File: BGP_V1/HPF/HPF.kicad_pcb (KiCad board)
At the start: 2 copper layers, 30 x 30 mm, 12 parts, among them P1 CONN_01X05, P2 CONN_01X06, U1 OPA2170

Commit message: Fixups
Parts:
- P2: moved to B.Cu
- moved P2 5.00 mm to (152.5, 53.0)
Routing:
- net /VF_1: track 11.3 -> 18.6 mm
- net /VP_1: track 29.4 -> 26.7 mm
- net Earth: track 2.40 -> 4.90 mm

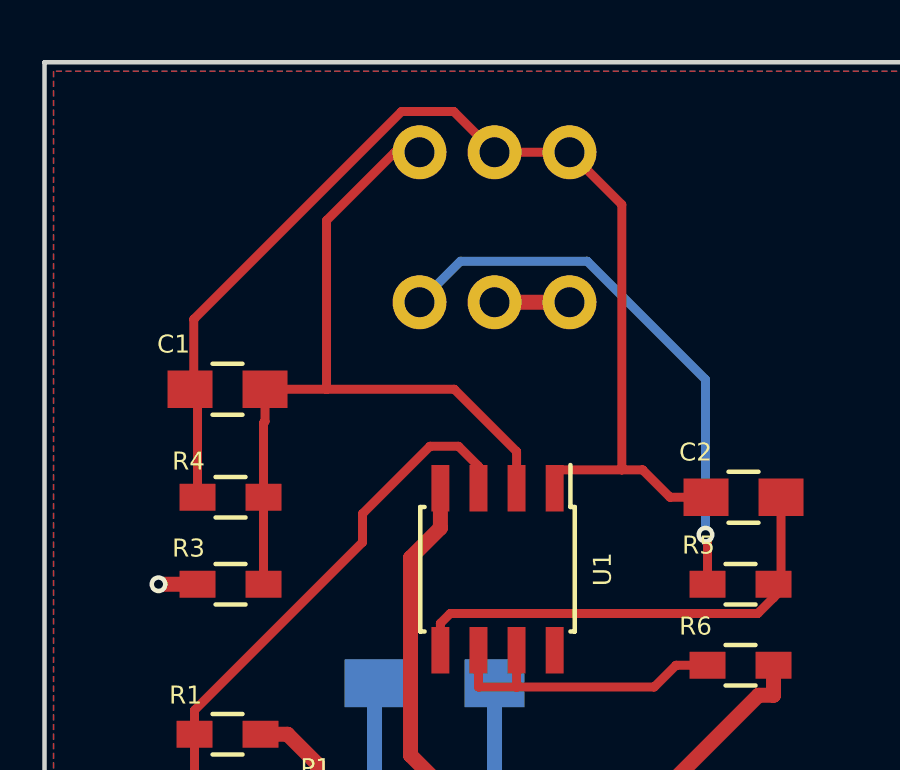
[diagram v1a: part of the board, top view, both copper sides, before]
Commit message: Pot fixups for silkscreen overlap
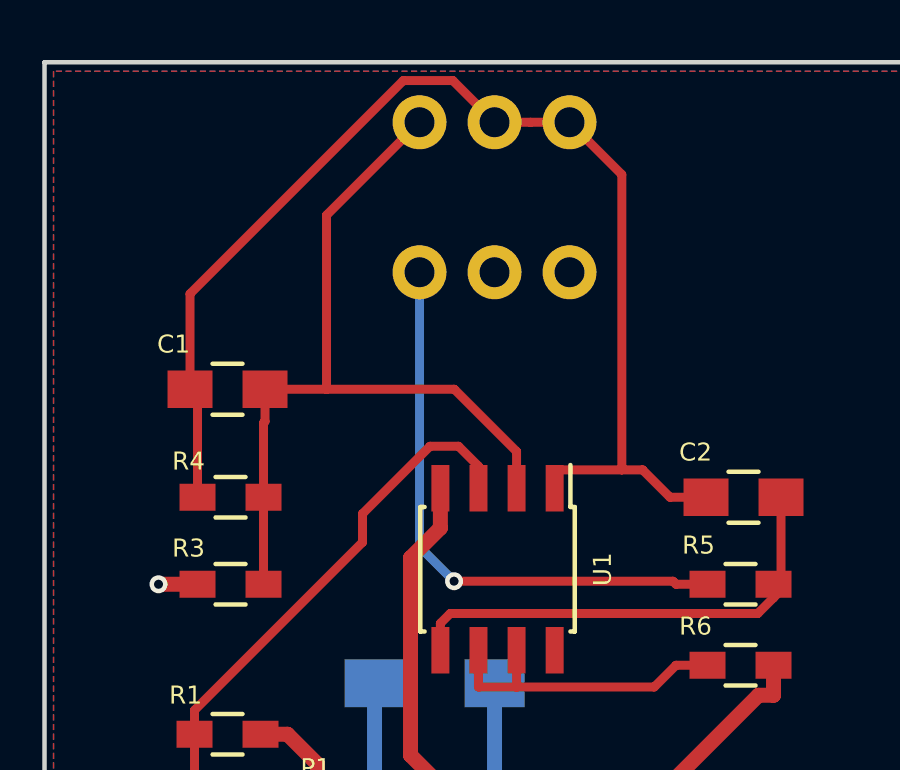
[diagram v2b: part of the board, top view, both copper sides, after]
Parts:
- R4: value 20k -> 24.9k
- moved P2 1.00 mm to (152.5, 52.0)
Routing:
- net Earth: track 4.90 -> 2.40 mm
- net /VP_2: track 39.5 -> 41.4 mm
- net /VF_1: track 18.6 -> 19.3 mm
- net /VP_1: track 26.7 -> 27.2 mm

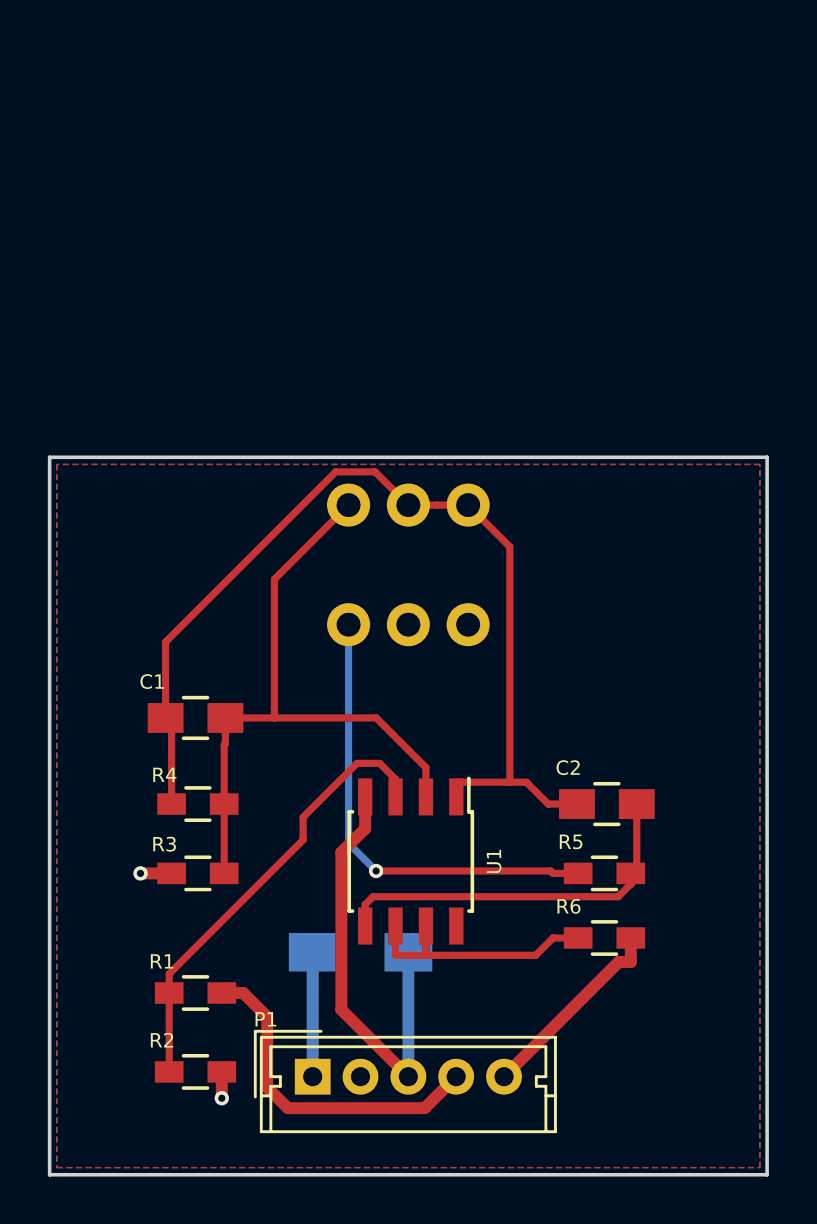
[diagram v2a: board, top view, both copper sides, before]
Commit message: Concentric pot fixups for 0_BT Stack and 1_HPF
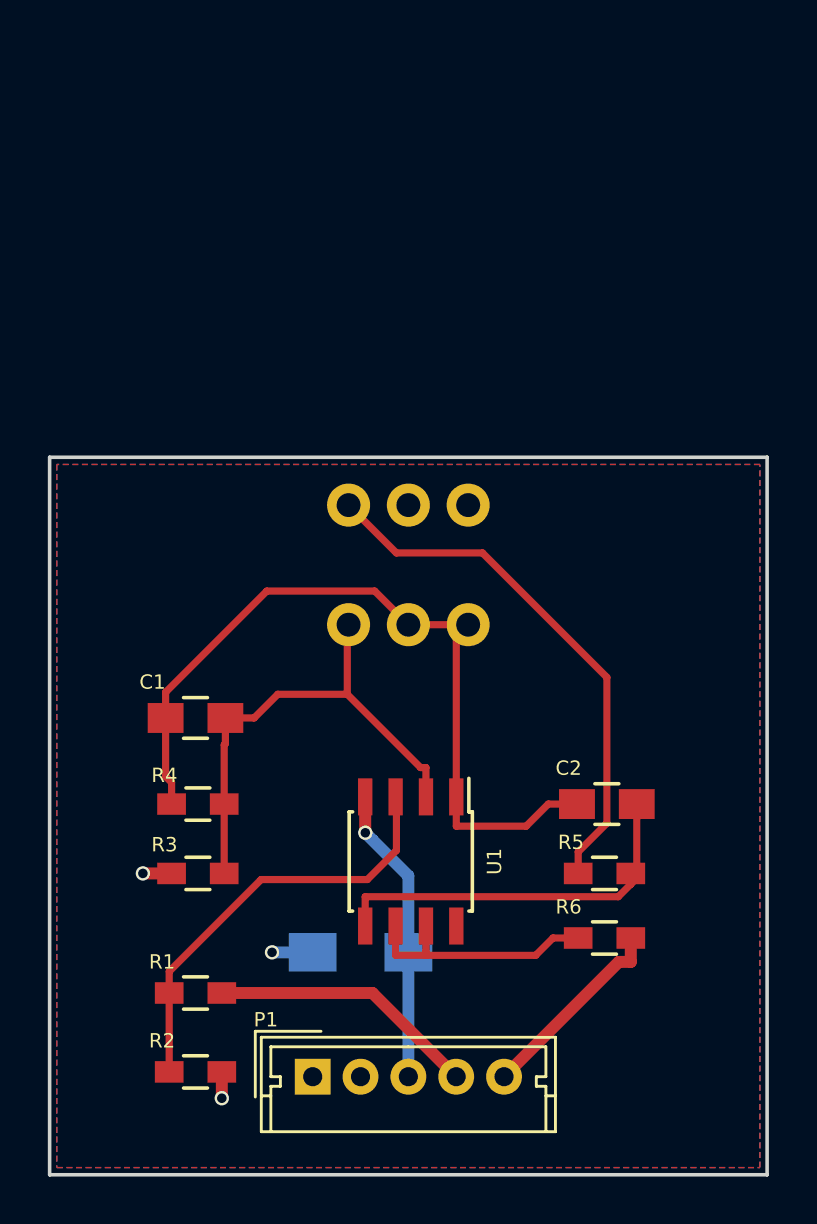
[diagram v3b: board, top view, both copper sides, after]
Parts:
- removed P2: CONN_01X06, LIBS:Potentiometer_Alps_RK097_Double_Vertical_Dual_Shaft
- added RV1: DUAL_POT, LIBS:Potentiometer_Alps_RK097_Double_Vertical_Dual_Shaft, B.Cu at (152.5, 52.0)
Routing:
- net /VP_2: track 41.4 -> 33.6 mm
- net /VP_1: track 27.2 -> 20.7 mm
- net /V-: track 18.5 -> 12.4 mm, vias 0 -> 1
- net /V+: track 5.20 -> 1.70 mm, vias 0 -> 1
- net /VF_1: track 19.3 -> 22.5 mm, vias 1 -> 0
- net /IN: track 14.1 -> 11.2 mm
- net Net-(R1-Pad1): track 18.8 -> 18.1 mm

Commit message: BOM for V1 BGP
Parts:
- moved C3 0.14 mm to (153.1, 70.6)
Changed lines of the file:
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@@
   (page A4)
   (layers
-    (0 F.Cu signal)
+    (0 F.Cu signal hide)
     (31 B.Cu signal)
     (32 B.Adhes user)
@@
     )
   )
-  (module Capacitors_SMD:C_1206_HandSoldering (layer B.Cu)
-    (at 153 70.7)
-    (descr "Capacitor SMD 1206, hand soldering")
-    (tags "capacitor 1206")
-    (attr smd)
-    (fp_text reference C3 (at 2.6 -1.6) (layer B.SilkS)
-      (effects (font (size 0.6 0.6) (thickness 0.15)) (justify mirror))
-    )
-    (fp_text value 10u (at 0 -2.3) (layer B.Fab) hide
-      (effects (font (size 0.6 0.6) (thickness 0.15)) (justify mirror))
-    )
-    (fp_line (start -3.3 1.15) (end 3.3 1.15) (layer B.CrtYd) (width 0.05))
-    (fp_line (start -3.3 -1.15) (end 3.3 -1.15) (layer B.CrtYd) (width 0.05))
-    (fp_line (start -3.3 1.15) (end -3.3 -1.15) (layer B.CrtYd) (width 0.05))
-    (fp_line (start 3.3 1.15) (end 3.3 -1.15) (layer B.CrtYd) (width 0.05))
-    (fp_line (start 1 1.025) (end -1 1.025) (layer B.SilkS) (width 0.15))
-    (fp_line (start -1 -1.025) (end 1 -1.025) (layer B.SilkS) (width 0.15))
-    (pad 1 smd rect (at -2 0) (size 2 1.6) (layers B.Cu B.Paste B.Mask)
-      (net 4 /V+))
-    (pad 2 smd rect (at 2 0) (size 2 1.6) (layers B.Cu B.Paste B.Mask)
-      (net 5 /V-))
-    (model Capacitors_SMD.3dshapes/C_1206_HandSoldering.wrl
-      (at (xyz 0 0 0))
-      (scale (xyz 1 1 1))
-      (rotate (xyz 0 0 0))
-    )
-  )
   (module Resistors_SMD:R_0603_HandSoldering (layer F.Cu)
     (at 146.1 72.4)
@@
       (rotate (xyz 0 0 0))
     )
+  )
+  (module Capacitors_SMD:C_1206_HandSoldering (layer B.Cu)
+    (at 153.1 70.6)
+    (descr "Capacitor SMD 1206, hand soldering")
+    (tags "capacitor 1206")
+    (attr smd)
+    (fp_text reference C3 (at 2.8 -1.6) (layer B.SilkS)
+      (effects (font (size 0.6 0.6) (thickness 0.15)) (justify mirror))
+    )
+    (fp_text value 10u (at 0 -2.3) (layer B.Fab) hide
+      (effects (font (size 0.6 0.6) (thickness 0.15)) (justify mirror))
+    )
+    (fp_line (start -3.3 1.15) (end 3.3 1.15) (layer B.CrtYd) (width 0.05))
+    (fp_line (start -3.3 -1.15) (end 3.3 -1.15) (layer B.CrtYd) (width 0.05))
+    (fp_line (start -3.3 1.15) (end -3.3 -1.15) (layer B.CrtYd) (width 0.05))
+    (fp_line (start 3.3 1.15) (end 3.3 -1.15) (layer B.CrtYd) (width 0.05))
+    (fp_line (start 1 1.025) (end -1 1.025) (layer B.SilkS) (width 0.15))
+    (fp_line (start -1 -1.025) (end 1 -1.025) (layer B.SilkS) (width 0.15))
+    (pad 1 smd rect (at -2 0) (size 2 1.6) (layers B.Cu B.Paste B.Mask)
+      (net 4 /V+))
+    (pad 2 smd rect (at 2 0) (size 2 1.6) (layers B.Cu B.Paste B.Mask)
+      (net 5 /V-))
+    (model Capacitors_SMD.3dshapes/C_1206_HandSoldering.wrl
+      (at (xyz 0 0 0))
+      (scale (xyz 1 1 1))
+      (rotate (xyz 0 0 0))
+    )

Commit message: Slight changes to Port layer placement - gerbers done
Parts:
- P1: moved to B.Cu
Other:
- board text added: "+"
- board text added: "-"
- board text added: "G"
- board text added: "I"
- board text added: "O"
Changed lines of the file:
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@@
     (links 26)
     (no_connects 0)
-    (area 139.924999 49.424999 170.075001 81.955)
+    (area 139.924999 49.424999 170.075001 80.075001)
     (thickness 1.6)
-    (drawings 9)
+    (drawings 14)
     (tracks 71)
     (zones 0)
@@
   (page A4)
   (layers
-    (0 F.Cu signal hide)
+    (0 F.Cu signal)
     (31 B.Cu signal)
     (32 B.Adhes user)
@@
     )
   )
-  (module Connectors_Molex:Molex_MicroLatch-53253-0570_05x2.00mm_Straight (layer F.Cu)
+  (module Connectors_Molex:Molex_MicroLatch-53253-0570_05x2.00mm_Straight (layer B.Cu)
     (at 151 75.9)
     (descr "Molex Micro-Latch connector, PN:53253-0570, top entry type, through hole")
     (tags "conn molex micro latch")
-    (fp_text reference P1 (at -1.96 -2.38) (layer F.SilkS)
-      (effects (font (size 0.6 0.6) (thickness 0.15)))
-    )
-    (fp_text value CONN_01X05 (at 3.63 5.2) (layer F.Fab) hide
-      (effects (font (size 0.6 0.6) (thickness 0.15)))
-    )
-    (fp_line (start -2 -1.5) (end -2 2.15) (layer F.Fab) (width 0.1))
-    (fp_line (start -2 2.15) (end 10 2.15) (layer F.Fab) (width 0.1))
-    (fp_line (start 10 2.15) (end 10 -1.5) (layer F.Fab) (width 0.1))
-    (fp_line (start 10 -1.5) (end -2 -1.5) (layer F.Fab) (width 0.1))
-    (fp_line (start -2.6 -2.1) (end -2.6 2.75) (layer F.CrtYd) (width 0.05))
-    (fp_line (start -2.6 2.75) (end 10.65 2.75) (layer F.CrtYd) (width 0.05))
-    (fp_line (start 10.65 2.75) (end 10.65 -2.1) (layer F.CrtYd) (width 0.05))
-    (fp_line (start 10.65 -2.1) (end -2.6 -2.1) (layer F.CrtYd) (width 0.05))
-    (fp_line (start -2.15 -1.65) (end -2.15 2.3) (layer F.SilkS) (width 0.12))
-    (fp_line (start -2.15 2.3) (end 10.15 2.3) (layer F.SilkS) (width 0.12))
-    (fp_line (start 10.15 2.3) (end 10.15 -1.65) (layer F.SilkS) (width 0.12))
-    (fp_line (start 10.15 -1.65) (end -2.15 -1.65) (layer F.SilkS) (width 0.12))
-    (fp_line (start 0.35 -1.9) (end -2.4 -1.9) (layer F.SilkS) (width 0.12))
-    (fp_line (start -2.4 -1.9) (end -2.4 0.85) (layer F.SilkS) (width 0.12))
-    (fp_line (start 0.35 -1.9) (end -2.4 -1.9) (layer F.Fab) (width 0.1))
-    (fp_line (start -2.4 -1.9) (end -2.4 0.85) (layer F.Fab) (width 0.1))
-    (fp_line (start -2.15 0.8) (end -1.75 0.8) (layer F.SilkS) (width 0.12))
-    (fp_line (start 10.15 0.8) (end 9.75 0.8) (layer F.SilkS) (width 0.12))
-    (fp_line (start 4 -1.25) (end -1.75 -1.25) (layer F.SilkS) (width 0.12))
-    (fp_line (start -1.75 -1.25) (end -1.75 0) (layer F.SilkS) (width 0.12))
-    (fp_line (start -1.75 0) (end -1.35 0) (layer F.SilkS) (width 0.12))
-    (fp_line (start -1.35 0) (end -1.35 0.4) (layer F.SilkS) (width 0.12))
-    (fp_line (start -1.35 0.4) (end -1.75 0.4) (layer F.SilkS) (width 0.12))
-    (fp_line (start -1.75 0.4) (end -1.75 2.3) (layer F.SilkS) (width 0.12))
-    (fp_line (start 4 -1.25) (end 9.75 -1.25) (layer F.SilkS) (width 0.12))
-    (fp_line (start 9.75 -1.25) (end 9.75 0) (layer F.SilkS) (width 0.12))
-    (fp_line (start 9.75 0) (end 9.35 0) (layer F.SilkS) (width 0.12))
-    (fp_line (start 9.35 0) (end 9.35 0.4) (layer F.SilkS) (width 0.12))
-    (fp_line (start 9.35 0.4) (end 9.75 0.4) (layer F.SilkS) (width 0.12))
-    (fp_line (start 9.75 0.4) (end 9.75 2.3) (layer F.SilkS) (width 0.12))
-    (fp_text user %R (at 4 1.5) (layer F.Fab) hide
-      (effects (font (size 0.6 0.6) (thickness 0.15)))
+    (fp_text reference P1 (at -2.5 2.38) (layer B.SilkS)
+      (effects (font (size 0.6 0.6) (thickness 0.15)) (justify mirror))
+    )
+    (fp_text value CONN_01X05 (at 3.63 -5.2) (layer B.Fab) hide
+      (effects (font (size 0.6 0.6) (thickness 0.15)) (justify mirror))
+    )
+    (fp_line (start -2 1.5) (end -2 -2.15) (layer B.Fab) (width 0.1))
+    (fp_line (start -2 -2.15) (end 10 -2.15) (layer B.Fab) (width 0.1))
+    (fp_line (start 10 -2.15) (end 10 1.5) (layer B.Fab) (width 0.1))
+    (fp_line (start 10 1.5) (end -2 1.5) (layer B.Fab) (width 0.1))
+    (fp_line (start -2.6 2.1) (end -2.6 -2.75) (layer B.CrtYd) (width 0.05))
+    (fp_line (start -2.6 -2.75) (end 10.65 -2.75) (layer B.CrtYd) (width 0.05))
+    (fp_line (start 10.65 -2.75) (end 10.65 2.1) (layer B.CrtYd) (width 0.05))
+    (fp_line (start 10.65 2.1) (end -2.6 2.1) (layer B.CrtYd) (width 0.05))
+    (fp_line (start -2.15 1.65) (end -2.15 -2.3) (layer B.SilkS) (width 0.12))
+    (fp_line (start -2.15 -2.3) (end 10.15 -2.3) (layer B.SilkS) (width 0.12))
+    (fp_line (start 10.15 -2.3) (end 10.15 1.65) (layer B.SilkS) (width 0.12))
+    (fp_line (start 10.15 1.65) (end -2.15 1.65) (layer B.SilkS) (width 0.12))
+    (fp_line (start 0.35 1.9) (end -2.4 1.9) (layer B.SilkS) (width 0.12))
+    (fp_line (start -2.4 1.9) (end -2.4 -0.85) (layer B.SilkS) (width 0.12))
+    (fp_line (start 0.35 1.9) (end -2.4 1.9) (layer B.Fab) (width 0.1))
+    (fp_line (start -2.4 1.9) (end -2.4 -0.85) (layer B.Fab) (width 0.1))
+    (fp_line (start -2.15 -0.8) (end -1.75 -0.8) (layer B.SilkS) (width 0.12))
+    (fp_line (start 10.15 -0.8) (end 9.75 -0.8) (layer B.SilkS) (width 0.12))
+    (fp_line (start 4 1.25) (end -1.75 1.25) (layer B.SilkS) (width 0.12))
+    (fp_line (start -1.75 1.25) (end -1.75 0) (layer B.SilkS) (width 0.12))
+    (fp_line (start -1.75 0) (end -1.35 0) (layer B.SilkS) (width 0.12))
+    (fp_line (start -1.35 0) (end -1.35 -0.4) (layer B.SilkS) (width 0.12))
+    (fp_line (start -1.35 -0.4) (end -1.75 -0.4) (layer B.SilkS) (width 0.12))
+    (fp_line (start -1.75 -0.4) (end -1.75 -2.3) (layer B.SilkS) (width 0.12))
+    (fp_line (start 4 1.25) (end 9.75 1.25) (layer B.SilkS) (width 0.12))
+    (fp_line (start 9.75 1.25) (end 9.75 0) (layer B.SilkS) (width 0.12))
+    (fp_line (start 9.75 0) (end 9.35 0) (layer B.SilkS) (width 0.12))
+    (fp_line (start 9.35 0) (end 9.35 -0.4) (layer B.SilkS) (width 0.12))
+    (fp_line (start 9.35 -0.4) (end 9.75 -0.4) (layer B.SilkS) (width 0.12))
+    (fp_line (start 9.75 -0.4) (end 9.75 -2.3) (layer B.SilkS) (width 0.12))
+    (fp_text user %R (at 4 -1.5) (layer B.Fab) hide
+      (effects (font (size 0.6 0.6) (thickness 0.15)) (justify mirror))
     )
     (pad 1 thru_hole rect (at 0 0) (size 1.5 1.5) (drill 0.8) (layers *.Cu *.Mask)
@@
     )
   )
+  (gr_text O (at 159 78.8) (layer B.SilkS)
+    (effects (font (size 0.6 0.6) (thickness 0.15)) (justify mirror))
+  )
+  (gr_text I (at 157 78.8) (layer B.SilkS)
+    (effects (font (size 0.6 0.6) (thickness 0.15)) (justify mirror))
+  )
+  (gr_text - (at 155 78.7) (layer B.SilkS)
+    (effects (font (size 0.6 0.6) (thickness 0.15)) (justify mirror))
+  )
+  (gr_text G (at 153 78.8) (layer B.SilkS)
+    (effects (font (size 0.6 0.6) (thickness 0.15)) (justify mirror))
+  )
+  (gr_text + (at 151 78.8) (layer B.SilkS)
+    (effects (font (size 0.6 0.6) (thickness 0.15)) (justify mirror))
+  )
   (gr_text "BGP V1.0\nHigh Pass Filter" (at 144.2 51.4) (layer B.SilkS)

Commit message: Slight changes to Port layer placement - gerbers done
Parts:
- moved P1 1.40 mm to (151.0, 77.3)
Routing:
- net /OUT: track 8.29 -> 10.0 mm
- net /V-: track 12.4 -> 14.0 mm
- net /IN: track 11.2 -> 11.8 mm
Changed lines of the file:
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@@
     (thickness 1.6)
     (drawings 14)
-    (tracks 71)
+    (tracks 73)
     (zones 0)
     (modules 12)
@@
   )
   (module Connectors_Molex:Molex_MicroLatch-53253-0570_05x2.00mm_Straight (layer B.Cu)
-    (at 151 75.9)
+    (at 151 77.3)
     (descr "Molex Micro-Latch connector, PN:53253-0570, top entry type, through hole")
     (tags "conn molex micro latch")
-    (fp_text reference P1 (at -2.5 2.38) (layer B.SilkS)
+    (fp_text reference P1 (at 11.2 -1.9) (layer B.SilkS)
       (effects (font (size 0.6 0.6) (thickness 0.15)) (justify mirror))
     )
@@
     )
   )
-  (gr_text O (at 159 78.8) (layer B.SilkS)
+  (gr_text O (at 159 74) (layer B.SilkS)
     (effects (font (size 0.6 0.6) (thickness 0.15)) (justify mirror))
   )
-  (gr_text I (at 157 78.8) (layer B.SilkS)
+  (gr_text I (at 157 74) (layer B.SilkS)
     (effects (font (size 0.6 0.6) (thickness 0.15)) (justify mirror))
   )
-  (gr_text - (at 155 78.7) (layer B.SilkS)
+  (gr_text - (at 155 73.9) (layer B.SilkS)
     (effects (font (size 0.6 0.6) (thickness 0.15)) (justify mirror))
   )
-  (gr_text G (at 153 78.8) (layer B.SilkS)
+  (gr_text G (at 153 74) (layer B.SilkS)
     (effects (font (size 0.6 0.6) (thickness 0.15)) (justify mirror))
   )
-  (gr_text + (at 151 78.8) (layer B.SilkS)
+  (gr_text + (at 151 74) (layer B.SilkS)
     (effects (font (size 0.6 0.6) (thickness 0.15)) (justify mirror))
   )
@@
   (segment (start 151 70.7) (end 149.300004 70.7) (width 0.5) (layer B.Cu) (net 4))
   (via (at 149.300004 70.7) (size 0.6) (drill 0.4) (layers F.Cu B.Cu) (net 4))
-  (segment (start 155 75.9) (end 155 70.7) (width 0.5) (layer B.Cu) (net 5))
+  (segment (start 155 77.3) (end 155 70.7) (width 0.5) (layer B.Cu) (net 5))
+  (segment (start 155 70.7) (end 155.1 70.6) (width 0.5) (layer B.Cu) (net 5))
   (segment (start 153.499999 65.999999) (end 153.2 65.7) (width 0.5) (layer B.Cu) (net 5))
   (segment (start 155 70.7) (end 155 67.5) (width 0.5) (layer B.Cu) (net 5))
@@
   (segment (start 145.1 67.4) (end 143.900006 67.4) (width 0.5) (layer F.Cu) (net 6))
   (via (at 143.900006 67.4) (size 0.6) (drill 0.4) (layers F.Cu B.Cu) (net 6))
-  (segment (start 153.5 72.4) (end 147.2 72.4) (width 0.5) (layer F.Cu) (net 7))
-  (segment (start 157 75.9) (end 153.5 72.4) (width 0.5) (layer F.Cu) (net 7))
-  (segment (start 163.7997 71.1003) (end 164.3 71.1003) (width 0.5) (layer F.Cu) (net 8))
-  (segment (start 159 75.9) (end 163.7997 71.1003) (width 0.5) (layer F.Cu) (net 8))
-  (segment (start 164.3 70.1) (end 164.3 71.1003) (width 0.5) (layer F.Cu) (net 8))
+  (segment (start 157 77.3) (end 152.1 72.4) (width 0.5) (layer F.Cu) (net 7))
+  (segment (start 152.1 72.4) (end 147.2 72.4) (width 0.5) (layer F.Cu) (net 7))
+  (segment (start 159 77.3) (end 160.06066 77.3) (width 0.5) (layer F.Cu) (net 8))
+  (segment (start 160.06066 77.3) (end 164.3 73.06066) (width 0.5) (layer F.Cu) (net 8))
+  (segment (start 164.3 73.06066) (end 164.3 71.05) (width 0.5) (layer F.Cu) (net 8))
+  (segment (start 164.3 71.05) (end 164.3 70.1) (width 0.5) (layer F.Cu) (net 8))
   (segment (start 154.465 64.2) (end 154.5 64.235) (width 0.3) (layer F.Cu) (net 9))
   (segment (start 154.5 64.235) (end 154.5 66.4409) (width 0.3) (layer F.Cu) (net 9))
